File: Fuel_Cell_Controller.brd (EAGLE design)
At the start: 203.2 x 163.8 mm, 148 parts, among them J1 BLUETOOTH, Q1 5.8A/30V/35mΩ, U1 MAX232PTH

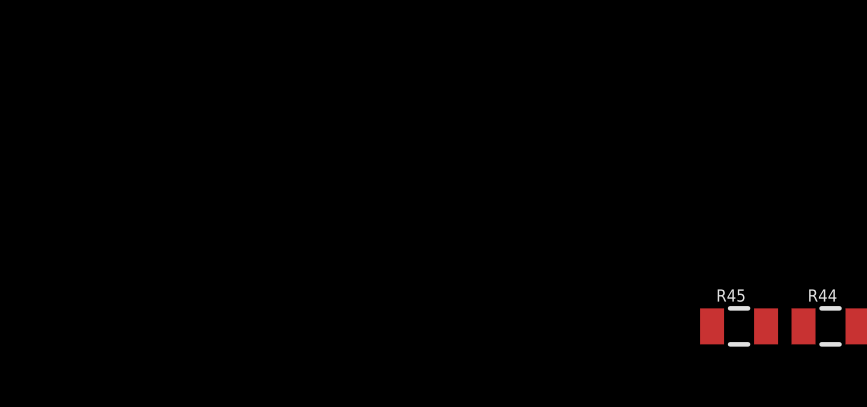
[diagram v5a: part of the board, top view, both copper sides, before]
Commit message: Added Pull Up resistors to thermistor inputs
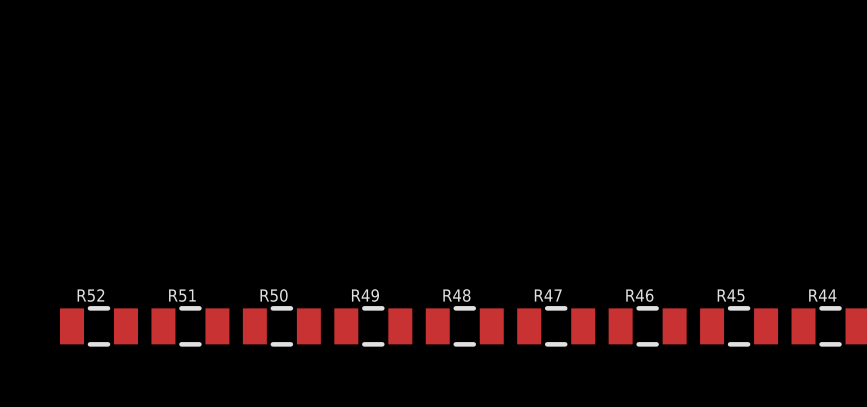
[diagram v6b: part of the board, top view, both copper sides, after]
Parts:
- added R46, R47, R48, R49, R50, R51, R52: 100kΩ, SparkFun-Passives:0805
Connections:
- net FCTEMP_2: now also R47.2
- net NUC_3V3: now also R46.1, R47.1, R48.1, R49.1, R50.2, R51.2, R52.2
- net TEMP_1: now also R48.2
- net TEMP_2: now also R49.2
- net TEMP_3: now also R50.1
- net TEMP_4: now also R51.1
- net TEMP_5: now also R52.1
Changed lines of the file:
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@@
 <element name="R44" library="SparkFun-Passives" package="0805" value="10kΩ" x="-41.656" y="-20.828"/>
 <element name="R45" library="SparkFun-Passives" package="0805" value="10kΩ" x="-44.704" y="-20.828"/>
+<element name="R46" library="SparkFun-Passives" package="0805" value="100kΩ" x="-47.752" y="-20.828"/>
+<element name="R47" library="SparkFun-Passives" package="0805" value="100kΩ" x="-50.8" y="-20.828"/>
+<element name="R48" library="SparkFun-Passives" package="0805" value="100kΩ" x="-53.848" y="-20.828"/>
+<element name="R49" library="SparkFun-Passives" package="0805" value="100kΩ" x="-56.896" y="-20.828"/>
+<element name="R50" library="SparkFun-Passives" package="0805" value="100kΩ" x="-59.944" y="-20.828"/>
+<element name="R51" library="SparkFun-Passives" package="0805" value="100kΩ" x="-62.992" y="-20.828"/>
+<element name="R52" library="SparkFun-Passives" package="0805" value="100kΩ" x="-66.04" y="-20.828"/>
 </elements>
 <signals>
@@
 <wire x1="5.842" y1="87.746" x2="5.842" y2="85.984715625" width="0.762" layer="1"/>
 <wire x1="5.842" y1="85.984715625" x2="5.588" y2="85.730715625" width="0.762" layer="1"/>
+<contactref element="R49" pad="1"/>
+<contactref element="R46" pad="1"/>
+<contactref element="R47" pad="1"/>
+<contactref element="R48" pad="1"/>
+<contactref element="R52" pad="2"/>
+<contactref element="R50" pad="2"/>
+<contactref element="R51" pad="2"/>
+<wire x1="-62.092" y1="-20.828" x2="-65.14" y2="-20.828" width="0" layer="19" extent="1-1"/>
+<wire x1="-59.044" y1="-20.828" x2="-62.092" y2="-20.828" width="0" layer="19" extent="1-1"/>
+<wire x1="-57.796" y1="-20.828" x2="-59.044" y2="-20.828" width="0" layer="19" extent="1-1"/>
+<wire x1="-54.748" y1="-20.828" x2="-57.796" y2="-20.828" width="0" layer="19" extent="1-1"/>
+<wire x1="-51.7" y1="-20.828" x2="-54.748" y2="-20.828" width="0" layer="19" extent="1-1"/>
+<wire x1="-48.652" y1="-20.828" x2="-51.7" y2="-20.828" width="0" layer="19" extent="1-1"/>
+<wire x1="3.048" y1="12.192" x2="-48.652" y2="-20.828" width="0" layer="19" extent="1-1"/>
 </signal>
 <signal name="OPEN_RST">
@@
 <wire x1="72.644" y1="8.128" x2="74.676" y2="10.16" width="0.762" layer="16"/>
 <wire x1="74.676" y1="10.16" x2="74.676" y2="23.368" width="0.762" layer="16"/>
+<contactref element="R47" pad="2"/>
+<wire x1="56.896" y1="8.128" x2="-49.9" y2="-20.828" width="0" layer="19" extent="1-16"/>
 </signal>
 <signal name="TEMP_1">
@@
 <wire x1="20.828" y1="59.055" x2="17.653" y2="59.055" width="0.762" layer="16"/>
 <wire x1="148.336" y1="71.628" x2="121.92" y2="45.212" width="0.762" layer="1"/>
+<contactref element="R48" pad="2"/>
+<wire x1="24.384" y1="21.336" x2="-52.948" y2="-20.828" width="0" layer="19" extent="1-16"/>
 </signal>
 <signal name="TEMP_2">
@@
 <wire x1="22.346284375" y1="40.010715625" x2="19.05" y2="40.010715625" width="0.762" layer="1"/>
 <wire x1="94.488" y1="44.196" x2="122.428" y2="44.196" width="0.762" layer="1"/>
+<contactref element="R49" pad="2"/>
+<wire x1="23.368" y1="20.828" x2="-55.996" y2="-20.828" width="0" layer="19" extent="1-16"/>
 </signal>
 <signal name="TEMP_3">
@@
 <wire x1="21.336" y1="42.545" x2="19.055715625" y2="42.545" width="0.762" layer="1"/>
 <wire x1="19.055715625" y1="42.545" x2="19.05" y2="42.550715625" width="0.762" layer="1"/>
+<contactref element="R50" pad="1"/>
+<wire x1="22.352" y1="20.32" x2="-60.844" y2="-20.828" width="0" layer="19" extent="1-16"/>
 </signal>
 <signal name="TEMP_4">
@@
 <wire x1="19.055715625" y1="37.465" x2="19.05" y2="37.470715625" width="0.762" layer="1"/>
 <wire x1="66.04" y1="15.24" x2="25.908" y2="15.24" width="0.762" layer="1"/>
+<contactref element="R51" pad="1"/>
+<wire x1="21.336" y1="19.812" x2="-63.892" y2="-20.828" width="0" layer="19" extent="1-16"/>
 </signal>
 <signal name="TEMP_5">
@@
 <wire x1="20.32" y1="56.515" x2="17.785715625" y2="56.515" width="0.762" layer="16"/>
 <wire x1="17.785715625" y1="56.515" x2="16.51" y2="57.790715625" width="0.762" layer="16"/>
+<contactref element="R52" pad="1"/>
+<wire x1="20.32" y1="19.304" x2="-66.94" y2="-20.828" width="0" layer="19" extent="1-16"/>
 </signal>
 <signal name="FCC_RELAY">

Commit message: ReRouted a few traces for resistors
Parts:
- moved R52 232.2 mm to (149.9, 64.5), flipped to the bottom, turned to 270 degrees
- moved R51 226.5 mm to (146.8, 64.5), flipped to the bottom, turned to 270 degrees
- moved R50 226.5 mm to (148.3, 68.1), flipped to the bottom, turned to 270 degrees
- moved R44 218.4 mm to (174.2, 12.2)
- moved R48 218.1 mm to (145.3, 68.1), flipped to the bottom, turned to 90 degrees
- moved R49 218.1 mm to (143.8, 64.5), flipped to the bottom, turned to 90 degrees
- moved R42 212.7 mm to (174.2, 14.2)
- moved R46 209.8 mm to (142.2, 68.1), flipped to the bottom, turned to 90 degrees
- moved R47 209.7 mm to (140.7, 64.5), flipped to the bottom, turned to 90 degrees
- moved R40 207.1 mm to (174.2, 16.3)
- moved R16 201.4 mm to (174.2, 18.3)
- moved R43 124.7 mm to (51.8, 65.0)
- moved R17 118.7 mm to (52.8, 67.6)
- moved R45 77.2 mm to (9.14, 34.5)
- moved R41 71.3 mm to (9.14, 37.1)
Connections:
- net FCTEMP_1: now also R46.2
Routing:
- net NUC_3V3: track 448.3 -> 508.5 mm
- net PRESSURE_2: track 260.7 -> 214.4 mm
- net _PRESSURE_4: track 0.00 -> 42.1 mm
- net _PRESSURE_2: track 0.00 -> 29.5 mm, vias 0 -> 1
- net PRESSURE_4: track 239.6 -> 215.2 mm, vias 2 -> 3
- net _PRESSURE_1: track 0.00 -> 16.1 mm
- net PRESSURE_1: track 187.6 -> 172.0 mm
- net _PRESSURE_3: track 0.00 -> 15.3 mm
- net PRESSURE_3: track 184.6 -> 174.4 mm
- net _CAP_CURR: track 215.0 -> 206.9 mm
- net FCTEMP_1: track 289.8 -> 291.5 mm, vias 9 -> 10
- net TEMP_5: track 256.2 -> 257.8 mm, vias 3 -> 4
- net TEMP_1: track 279.1 -> 280.4 mm, vias 3 -> 4
- net TEMP_3: track 250.4 -> 251.6 mm, vias 6 -> 7
- net TEMP_2: track 233.6 -> 233.7 mm, vias 4 -> 5
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
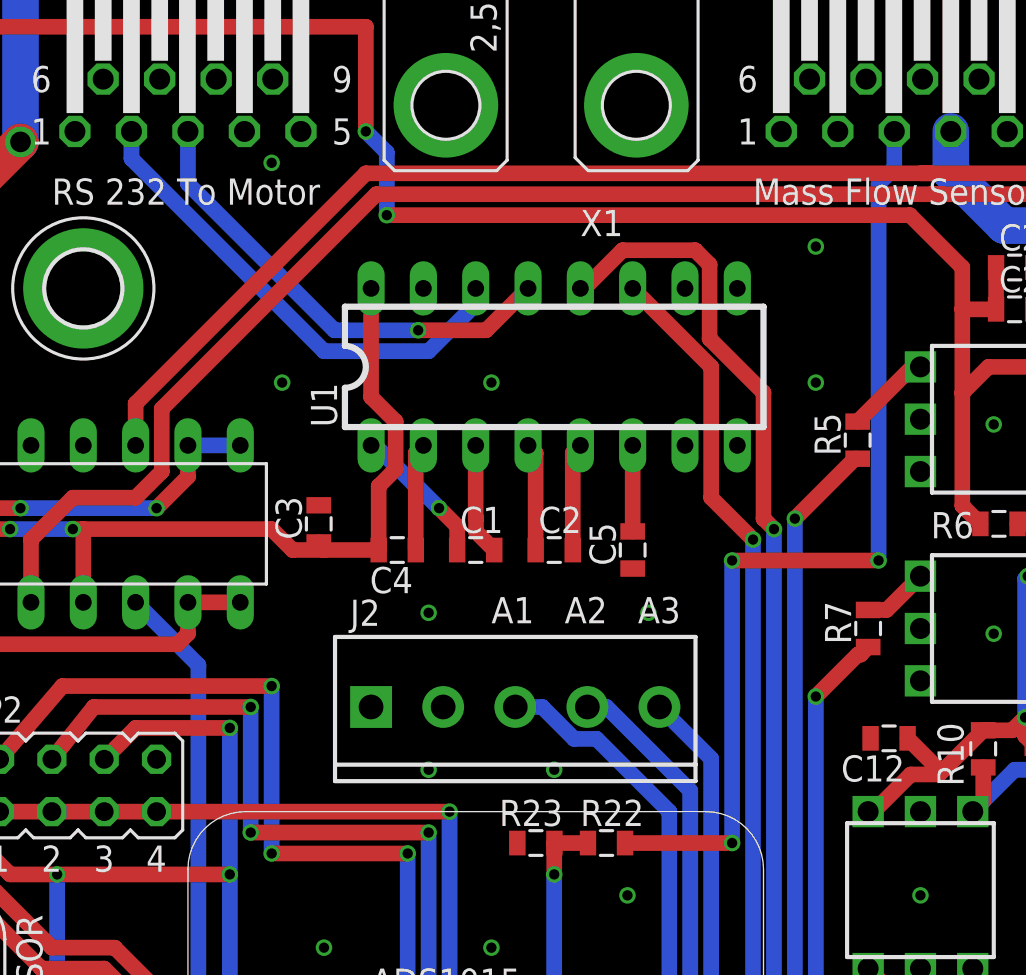
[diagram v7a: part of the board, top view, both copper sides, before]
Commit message: Changed DSUB connector pinouts
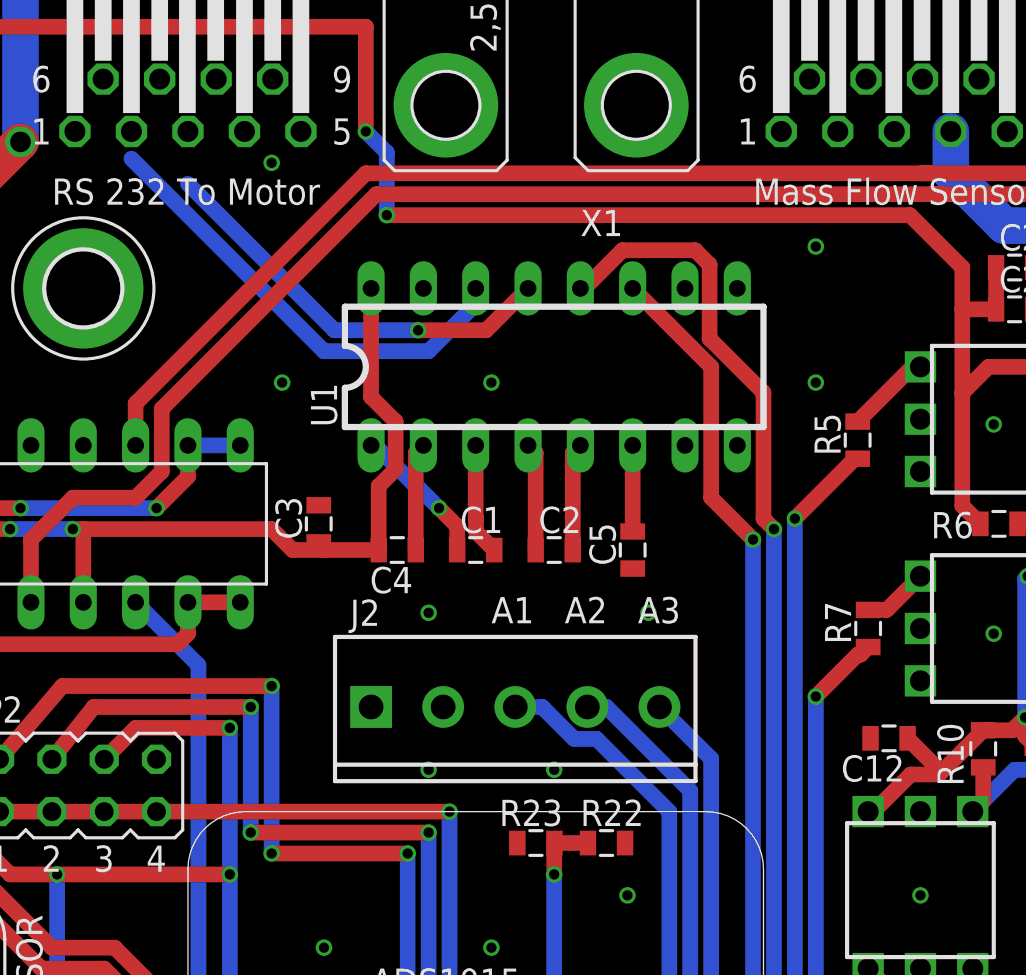
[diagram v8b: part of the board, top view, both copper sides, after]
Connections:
- removed net N$22: R22.2, X1.3
- new net N$15: R22.2, X1.2
- net FROM_MOTOR: now also X2.2; no longer X2.3
- net GND: now also X1.3; no longer X1.2
- net TO_MOTOR: now also X2.3; no longer X2.2
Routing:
- net N$22: track 47.2 -> 0.00 mm, vias 3 -> 0
- net FROM_MOTOR: track 22.8 -> 20.3 mm
- net TO_MOTOR: track 23.6 -> 22.3 mm
